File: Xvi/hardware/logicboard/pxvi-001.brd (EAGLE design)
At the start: 100 x 75 mm, 90 parts, among them J1 MKR, J4 QWIIC_RIGHT_ANGLE, J5 SPI, J6 QWIIC_RIGHT_ANGLE, J7 DIN5, K1 G5V1, Q1 60V/32A/35mΩ, Q10 60V/32A/35mΩ, Q11 60V/32A/35mΩ, Q12 60V/32A/35mΩ, Q13 60V/32A/35mΩ, Q14 60V/32A/35mΩ, Q15 60V/32A/35mΩ, Q16 60V/32A/35mΩ, Q2 60V/32A/35mΩ, Q3 60V/32A/35mΩ, Q4 60V/32A/35mΩ, Q5 60V/32A/35mΩ, Q6 60V/32A/35mΩ, Q7 60V/32A/35mΩ, Q8 60V/32A/35mΩ, Q9 60V/32A/35mΩ, T1 2SC1815, U1 DS18B20, X1 ADAFRUIT-PCA9685, X2 MKDSN1,5/2-5,08

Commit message: Wired.
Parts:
- added C25: 10n, resistor:C025-024X044
- added D2: (no value), SparkFun-DiscreteSemi:DIODE-1N4148
- moved J3 73.0 mm to (25.0, 8.50), turned to 180 degrees
- moved J6 60.0 mm to (75.5, 6.00), flipped to the bottom
- moved J4 54.0 mm to (62.5, 6.00), flipped to the bottom
- moved C8 41.1 mm to (9.00, 65.5), turned to 0 degrees
- moved J1 14.0 mm to (11.0, 6.00)
- moved DD1 2.06 mm to (72.0, 52.0)
- moved DD10 2.06 mm to (86.5, 47.0)
- moved DD11 2.06 mm to (86.5, 42.0)
- moved DD12 2.06 mm to (86.5, 37.0)
- moved DD13 2.06 mm to (86.5, 32.0)
- moved DD14 2.06 mm to (86.5, 27.0)
- moved DD15 2.06 mm to (86.5, 22.0)
- moved DD16 2.06 mm to (86.5, 17.0)
- moved DD2 2.06 mm to (72.0, 47.0)
- moved DD3 2.06 mm to (72.0, 42.0)
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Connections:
- net N$1: now also C25.2, D2.A
- net VCC: now also C25.1, D2.C
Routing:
- net LD00: track 93.6 -> 216.7 mm, vias 1 -> 8
- net V+: track 405.4 -> 311.9 mm, vias 14 -> 12
- net LD03: track 54.3 -> 123.1 mm, vias 4 -> 10
- net PWM10: track 74.8 -> 135.1 mm, vias 3 -> 2
- net LD13: track 58.5 -> 116.4 mm, vias 1 -> 3
- net VCC: track 347.3 -> 400.0 mm, vias 7 -> 10
- net PWM12: track 72.5 -> 121.7 mm, vias 5 -> 6
- net SCL: track 154.5 -> 201.0 mm
- net PWM11: track 67.7 -> 111.3 mm, vias 2 -> 1
- net SDA: track 172.9 -> 210.0 mm, vias 4 -> 1
- net LD10: track 99.2 -> 64.2 mm, vias 3 -> 5
- net LD04: track 30.3 -> 59.9 mm, vias 1 -> 3
- net LD14: track 70.3 -> 42.1 mm
- net LD12: track 74.0 -> 45.9 mm, vias 4 -> 2
- net LD08: track 61.3 -> 88.4 mm
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
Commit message: Wired.
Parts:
- removed J4, J6: QWIIC_RIGHT_ANGLE, SparkFun-Connectors:JST04_1MM_RA
- moved U$1 34.0 mm to (31.0, 37.5), flipped to the bottom, turned to 270 degrees
- moved D1 5.02 mm to (94.0, 57.5)
- moved C3 2.55 mm to (94.0, 52.5)
- moved C4 2.55 mm to (94.0, 55.0)
- moved C6 1.00 mm to (35.5, 71.5), turned to 0 degrees
- moved LOGO1 1.00 mm to (40.5, 7.00)
- moved RN3 1.00 mm to (26.5, 71.5)
- moved C7 0.71 mm to (35.5, 3.50), turned to 180 degrees
- moved DD10 0.71 mm to (86.0, 47.5)
- moved DD11 0.71 mm to (86.0, 42.5)
- moved DD12 0.71 mm to (86.0, 37.5)
- moved DD13 0.71 mm to (86.0, 32.5)
- moved DD14 0.71 mm to (86.0, 27.5)
- moved DD15 0.71 mm to (86.0, 22.5)
- moved DD16 0.71 mm to (86.0, 17.5)
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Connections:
- net GND: no longer J4.1, J6.1
- net SCL: no longer J4.4, J6.4
- net SDA: no longer J4.3, J6.3
- net VCC: no longer J4.2, J6.2
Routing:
- net LD00: track 216.7 -> 75.0 mm, vias 8 -> 3
- net LD11: track 58.8 -> 160.5 mm, vias 0 -> 9
- net LD13: track 116.4 -> 44.5 mm, vias 3 -> 4
- net SDA: track 210.0 -> 146.9 mm, vias 1 -> 3
- net SCL: track 201.0 -> 139.6 mm, vias 6 -> 1
- net PWM12: track 121.7 -> 174.3 mm, vias 6 -> 3
- net PWM11: track 111.3 -> 66.5 mm, vias 1 -> 2
- net PWM10: track 135.1 -> 91.2 mm, vias 2 -> 3
- net LD09: track 72.1 -> 113.6 mm, vias 5 -> 4
- net GND: track 527.4 -> 493.4 mm, vias 11 -> 6
- net LD03: track 123.1 -> 90.3 mm, vias 10 -> 4
- net MOSI: track 66.9 -> 98.2 mm, vias 3 -> 2
- net LD02: track 53.7 -> 82.3 mm, vias 2 -> 4
- net GPIO0: track 65.4 -> 93.5 mm, vias 2 -> 0
- net D7GATE: track 110.5 -> 84.2 mm, vias 0 -> 2
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
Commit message: Re-routed.
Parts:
- turned K1 to 270 degrees
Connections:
- net N$1 renamed VRLY
- net N$4 renamed FAN
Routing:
- net LD11: track 160.5 -> 58.8 mm, vias 9 -> 4
- net PWM12: track 174.3 -> 80.7 mm
- net VCC: track 374.3 -> 320.6 mm, vias 3 -> 2
- net LD13: track 44.5 -> 79.4 mm, vias 4 -> 2
- net PWM08: track 106.1 -> 77.5 mm, vias 2 -> 4
- net LD03: track 90.3 -> 62.7 mm, vias 4 -> 5
- net PWM11: track 66.5 -> 91.3 mm, vias 2 -> 5
- net LD09: track 113.6 -> 90.5 mm
- net LD04: track 34.8 -> 57.0 mm, vias 3 -> 2
- net SCL: track 139.6 -> 157.3 mm, vias 1 -> 2
- net PWM14: track 90.3 -> 107.3 mm, vias 5 -> 0
- net MOSI: track 98.2 -> 81.9 mm
- net LD08: track 98.8 -> 84.5 mm, vias 3 -> 12
- net PWM13: track 82.4 -> 96.6 mm, vias 3 -> 1
- net LD01: track 80.2 -> 94.0 mm, vias 3 -> 6
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
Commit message: Silk.
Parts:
- moved J2 0.50 mm to (50.0, 66.5)
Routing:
- net PWM09: track 80.5 -> 129.7 mm, vias 6 -> 1
- net PWM14: track 107.3 -> 75.9 mm, vias 0 -> 4
- net LD10: track 63.1 -> 89.9 mm
- net LD04: track 57.0 -> 81.1 mm
- net THS: track 145.0 -> 121.2 mm, vias 0 -> 3
- net LD08: track 84.5 -> 61.6 mm, vias 12 -> 5
- net SCL: track 157.3 -> 135.7 mm
- net GND: track 494.7 -> 473.7 mm, vias 8 -> 7
- net LD14: track 59.3 -> 42.0 mm
- net PWM01: track 50.2 -> 66.4 mm, vias 0 -> 1
- net LD13: track 79.4 -> 63.5 mm, vias 2 -> 3
- net LD03: track 62.7 -> 77.5 mm
- net GPIO0: track 81.0 -> 67.3 mm, vias 3 -> 0
- net PWM13: track 96.6 -> 83.3 mm, vias 1 -> 2
- net PWM11: track 91.3 -> 78.1 mm, vias 5 -> 3
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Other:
- board text added: "D7"
- board text added: "GND"
- board text added: "Grove"
- board text added: "LightDrive"
- board text added: "MIDI-IN"
- board text added: "SCL"
- board text added: "SDA"
- board text added: "THS"
- board text added: "Vcc"

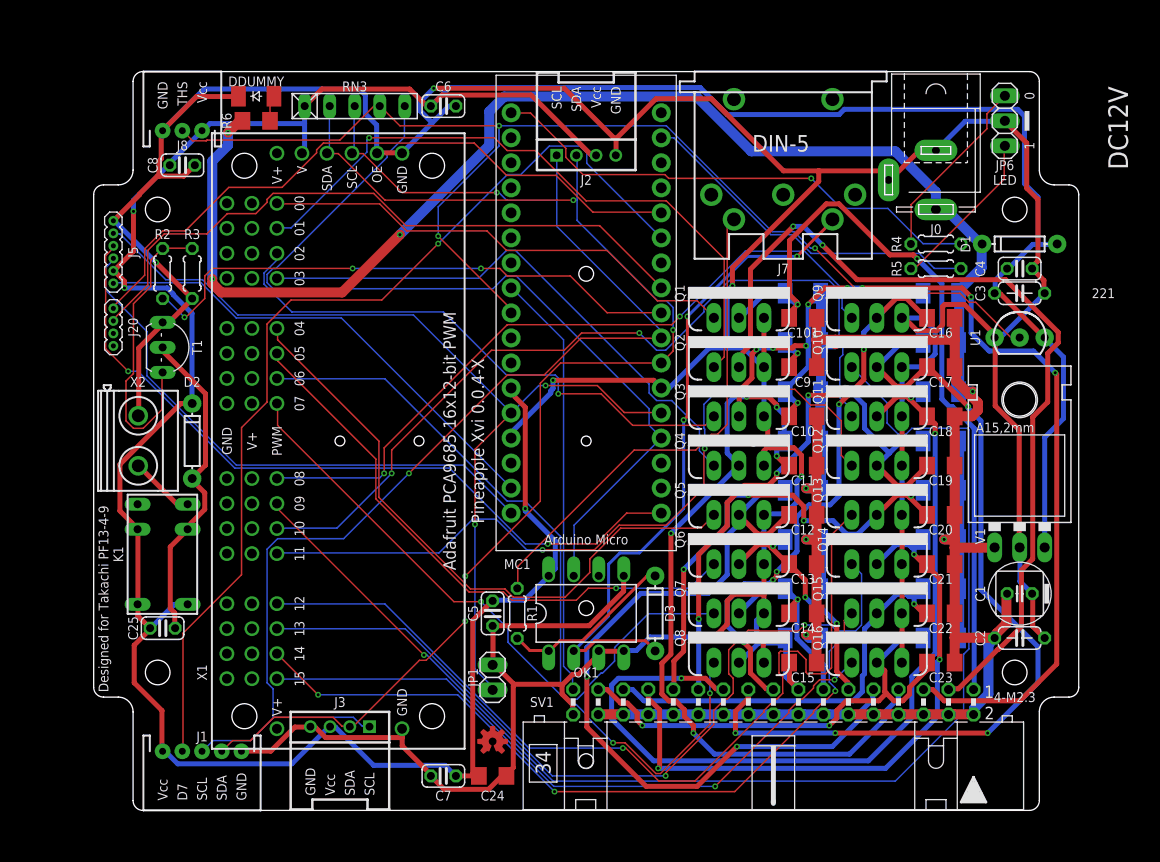
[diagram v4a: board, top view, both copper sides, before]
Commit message: GND pattern.
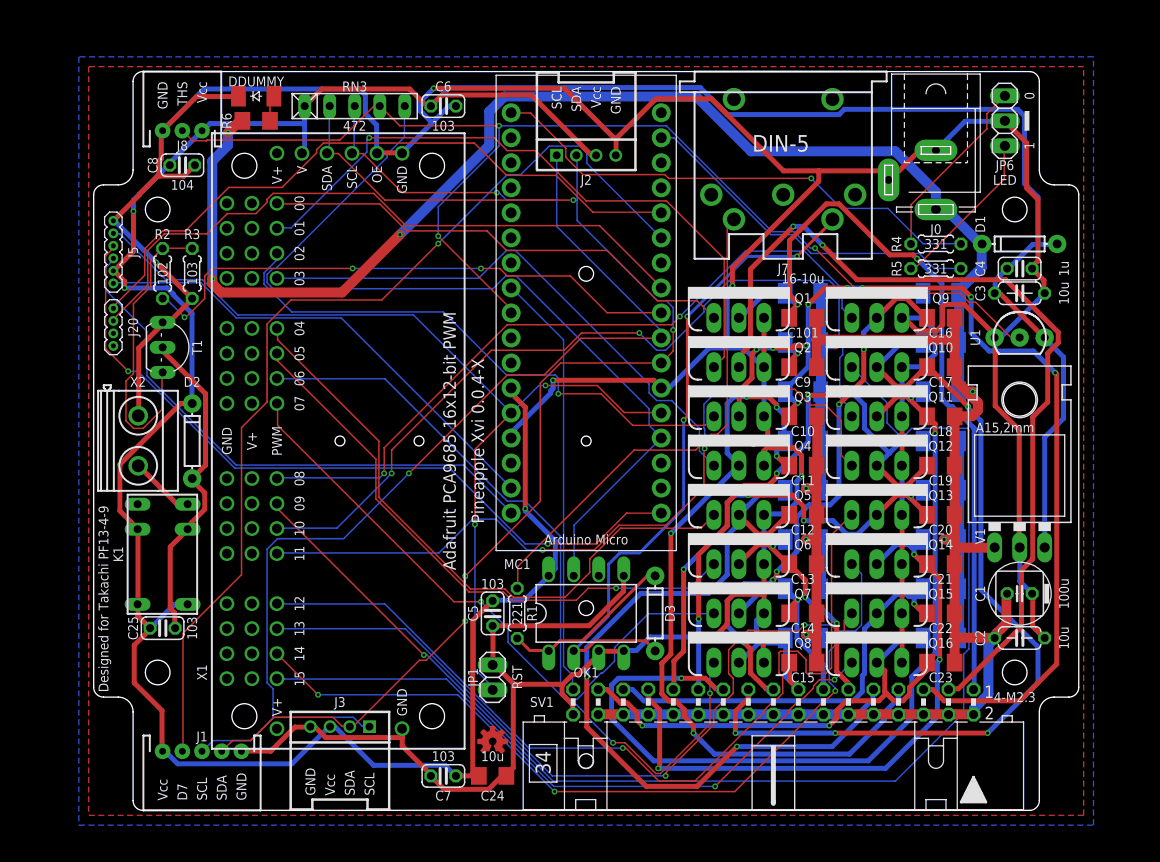
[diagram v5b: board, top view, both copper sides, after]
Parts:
- R3: value 1k -> 10k
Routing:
- added copper zone on layer 1, net GND
- added copper zone on layer 16, net GND
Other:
- board text added: "100u"
- board text added: "102"
- board text added: "103"
- board text added: "104"
- board text added: "10u"
- board text added: "16-10u"
- board text added: "1u"
- board text added: "331"
- board text added: "472"
- board text added: "RST"

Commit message: Silk.
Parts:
- removed C25: 10n, resistor:C025-024X044
- removed R3: 10k, resistor:0204/5
- added C102: (no value), rcl:C3216
- added R13: (no value), rcl:R3216
- C9: value (none) -> 10n; device rcl:C3216 -> resistor:C025-024X044
- R1: value 220 -> 1k
- R2: value 1k -> 10k
- R6: value (none) -> 220; device rcl:R3216 -> resistor:0204/5
- moved C9 70.2 mm to (7.00, 18.5), turned to 0 degrees
- moved R6 56.6 mm to (43.0, 20.0), turned to 90 degrees
- moved R1 49.9 mm to (7.00, 54.5)
- moved R2 3.00 mm to (10.0, 54.5)
- renumbered C10 to C103, C11 to C104, C12 to C105, C13 to C106, C14 to C107, C15 to C108, C16 to C109, C17 to C110, C18 to C111, C19 to C112, C20 to C113, C21 to C114, C22 to C115, C23 to C116, C24 to C100, DD1 to D101, DD10 to D110, DD11 to D111, DD12 to D112, DD13 to D113, DD14 to D114, DD15 to D115, DD16 to D116, DD2 to D102, DD3 to D103, DD4 to D104, DD5 to D105, DD6 to D106, DD7 to D107, DD8 to D108, DD9 to D109, DDUMMY to D100LED, J2 to J21, J3 to J22, J8 to J10, JP1 to JP0, SV1 to SV4, X1 to U2
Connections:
- net GND: now also R2.1; no longer R3.1
- net LD01: now also C102.2; no longer C9.2
- net MISND: now also R6.2; no longer R1.2
- net MISNDA: now also R6.1; no longer R1.1
- net N$2: now also R1.2; no longer R3.2
- net N$3: now also R13.1; no longer R6.1
- net RLY: now also R1.1; no longer R2.1
- net V+: now also C102.1, R13.2; no longer C9.1, R6.2
- net VCC: now also C9.1; no longer C25.1
- net VRLY: now also C9.2; no longer C25.2
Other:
- board text added: "16-30N06"
- board text added: "7805"
- board text added: "C1815"
- board text added: "DS18B20+"
- board text added: "FAN (DC5V)"
- board text added: "G5V-1"
- board text added: "TLP2630"
